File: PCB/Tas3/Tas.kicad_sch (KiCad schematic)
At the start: 28 parts, among them J1 Shelly 1, J2 Conn_01x07, J3 USB-C, U1 MD8942, U2 Barcode, U3 CH340X, U4 ZXGD3009E6, U5 ZXGD3009E6

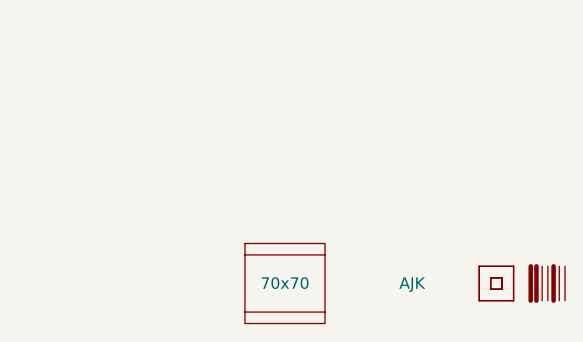
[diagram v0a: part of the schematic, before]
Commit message: Changed for cheaper assembly
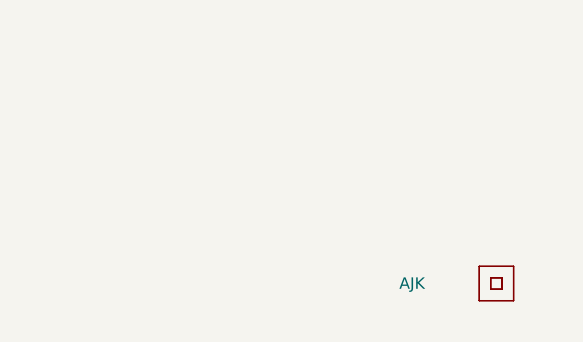
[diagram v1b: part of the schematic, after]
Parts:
- removed PCB1: 70x70, RevK:PCB7070, symbol RevK:PCB
- removed U2: Barcode, RevK:EAN-5060634238014, symbol RevK:Barcode
- removed V1, V2: ~, RevK:VCUT70, symbol RevK:VCUT
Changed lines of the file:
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@@
-    )
-  )
-  (symbol (lib_id "RevK:PCB") (at 245.745 172.72 0) (unit 1)
-    (in_bom no) (on_board yes) (dnp no)
-    (property "Reference" "PCB1" (at 245.745 182.88 0)
-      (effects (font (size 1.27 1.27)) hide)
-    )
-    (property "Value" "70x70" (at 245.745 172.72 0)
-      (effects (font (size 1.27 1.27)))
-    )
-    (property "Footprint" "RevK:PCB7070" (at 245.745 167.005 0)
-      (effects (font (size 1.27 1.27)) hide)
-    )
-    (property "Datasheet" "" (at 245.745 172.72 0)
-      (effects (font (size 1.27 1.27)) hide)
-    )
-    (instances
-      (project "Tas"
-        (path "/42713045-fffd-4b2d-ae1e-7232d705fb12"
-          (reference "PCB1") (unit 1)
-        )
-      )
     )
   )
@@
         (path "/825c70b0-4860-42b7-97dc-86bfa46e06fd"
           (reference "R8") (unit 1)
-        )
-      )
-    )
-  )
-  (symbol (lib_id "RevK:VCUT") (at 245.745 175.895 0) (unit 1)
-    (in_bom no) (on_board yes) (dnp no) (fields_autoplaced)
-    (property "Reference" "V1" (at 245.745 174.625 0)
-      (effects (font (size 1.27 1.27)) hide)
-    )
-    (property "Value" "~" (at 245.745 175.895 0)
-      (effects (font (size 1.27 1.27)))
-    )
-    (property "Footprint" "RevK:VCUT70" (at 245.745 177.165 0)
-      (effects (font (size 1.27 1.27)) hide)
-    )
-    (property "Datasheet" "" (at 245.745 175.895 0)
-      (effects (font (size 1.27 1.27)) hide)
-    )
-    (property "Sim.Enable" "0" (at 245.745 175.895 0)
-      (effects (font (size 1.27 1.27)) hide)
-    )
-    (instances
-      (project "Tas"
-        (path "/42713045-fffd-4b2d-ae1e-7232d705fb12"
-          (reference "V1") (unit 1)
-        )
-      )
-      (project "Reference"
-        (path "/825c70b0-4860-42b7-97dc-86bfa46e06fd"
-          (reference "V1") (unit 1)
-        )
-      )
-    )
-  )
-  (symbol (lib_id "RevK:VCUT") (at 245.745 169.545 0) (unit 1)
-    (in_bom no) (on_board yes) (dnp no) (fields_autoplaced)
-    (property "Reference" "V2" (at 245.745 168.275 0)
-      (effects (font (size 1.27 1.27)) hide)
-    )
-    (property "Value" "~" (at 245.745 169.545 0)
-      (effects (font (size 1.27 1.27)))
-    )
-    (property "Footprint" "RevK:VCUT70" (at 245.745 170.815 0)
-      (effects (font (size 1.27 1.27)) hide)
-    )
-    (property "Datasheet" "" (at 245.745 169.545 0)
-      (effects (font (size 1.27 1.27)) hide)
-    )
-    (property "Sim.Enable" "0" (at 245.745 169.545 0)
-      (effects (font (size 1.27 1.27)) hide)
-    )
-    (instances
-      (project "Tas"
-        (path "/42713045-fffd-4b2d-ae1e-7232d705fb12"
-          (reference "V2") (unit 1)
-        )
-      )
-      (project "Reference"
-        (path "/825c70b0-4860-42b7-97dc-86bfa46e06fd"
-          (reference "V1") (unit 1)
         )
       )
@@
         )
       )
-    )
-  )
-  (symbol (lib_id "RevK:Barcode") (at 274.955 172.72 0) (unit 1)
-    (in_bom no) (on_board yes) (dnp no) (fields_autoplaced)
-    (property "Reference" "U2" (at 274.955 175.895 0)
-      (effects (font (size 1.27 1.27)) hide)
-    )
-    (property "Value" "Barcode" (at 274.955 177.8 0)
-      (effects (font (size 1.27 1.27)) hide)
-    )
-    (property "Footprint" "RevK:EAN-5060634238014" (at 274.32 173.355 0)
-      (effects (font (size 1.27 1.27)) hide)
-    )
-    (property "Datasheet" "" (at 274.32 173.355 0)
-      (effects (font (size 1.27 1.27)) hide)
-    )
-    (property "Note" "Non part, PCB printed" (at 274.955 167.005 0)
-      (effects (font (size 1.27 1.27)) hide)
-    )
-    (instances
-      (project "USBA"
-        (path "/2d210a96-f81f-42a9-8bf4-1b43c11086f3"
-          (reference "U2") (unit 1)
-        )
-      )
-      (project "Tas"
-        (path "/42713045-fffd-4b2d-ae1e-7232d705fb12"
-          (reference "U2") (unit 1)
-        )
-      )
-      (project "Faikin"
-        (path "/46c350bb-7de4-4e81-aafd-4af55e37aab0"
-          (reference "U4") (unit 1)
-        )
-      )
-      (project "Reference"
-        (path "/825c70b0-4860-42b7-97dc-86bfa46e06fd"
-          (reference "U3") (unit 1)
-        )
-      )

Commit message: Changed voltage...
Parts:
- R4: value 40k2 -> 34k4
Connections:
- net RST+: now also J2.4 (Pin_4)
- net VBUS: now also U3.7 (VCC)
- net +3V3 renamed +3V8
- net +3V8: no longer C5.1, J2.4 (Pin_4), U3.10 (V3), U3.7 (VCC)
- new net: C5.1, U3.10 (V3)
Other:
- note added: "Aiming for 3.8V due to driver drop"
- note added: "DOES NOT WORK AT 3V3 The 0.8 to 0.4 drop on high and 0.2 to 0.5 on low are an issue. Low is probably OK, but high means needs drive of at least 0.5V higher. Measured was 0.45V drop."
- note added: "New resistor values"
- moved on the sheet: C5

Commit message: Try again, as ordered.
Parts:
- removed U4, U5: ZXGD3009E6, RevK:SOT-23-6, symbol Driver_FET:ZXGD3009E6
- added Q1: AP2003, RevK:SOT-23-6, symbol Transistor_FET:DMC3071LVT
- added U2: 74LVC1G07, RevK:SOT-353_SC-70-5, symbol 74xGxx:NC7SZ125M5X
- added U4: 74LVC1G06SE-7, RevK:SOT-353_SC-70-5, symbol 74xGxx:NC7SVU04P5X
- D1: JLCPCB Rotation Offset -90 -> 0; LCSC Part # C68987 -> C96225
- R4: value 34k4 -> 39k2
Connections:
- net +3V8 is gone; now on net +3V3: D1.2 (K2), D1.5 (K4), D5.4 (A), U1.8 (VOUT)
- net B: now also U2.4 (Y)
- net GND: now also Q1.5 (S), U2.1 (~{OE}), U2.3 (GND), U4.3 (GND)
- net GPIO0: now also U2.2 (A)
- net RST: now also U4.2
- net RST+: now also Q1.4 (D), Q1.6 (D); no longer J2.4 (Pin_4)
- net VBUS: no longer U3.7 (VCC)
- net +3V3: now reaches C5.1, U3.10 (V3)
- net +3V3: now also J2.4 (Pin_4), U3.7 (VCC), Q1.2 (S), U2.5 (VCC), U4.5 (VCC)
- new net: Q1.1 (G), Q1.3 (G), U4.4
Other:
- note removed: "Aiming for 3.8V due to driver drop"
- note removed: "Cannot connect GPIO0 directly as internal pulls in shelly upset CH340X"
- note removed: "DOES NOT WORK AT 3V3 The 0.8 to 0.4 drop on high and 0.2 to 0.5 on low are an issue. Low is probably OK, but high means needs drive of at least 0.5V higher. Measured was 0.45V drop."
- note removed: "New resistor values"
- moved on the sheet: C1, C5, C6, C7, D1A, D1B, D5, J1, J2, J3, L2, R1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

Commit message: Maybe Nth time lucky
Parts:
- added C2: 100nF, RevK:C_0402, symbol Device:C
- added R5, R6: 4K7, RevK:R_0402, symbol Device:R
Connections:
- net +3V3: now also R5.1, R6.1; no longer U3.10 (V3), U3.7 (VCC)
- net B: now also R6.2
- net GND: now also C2.1
- net VBUS: now also U3.7 (VCC)
- net at Q1.1 (G), Q1.3 (G), U4.4: now also R5.2
- new net: C2.2, U3.10 (V3)
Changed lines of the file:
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@@
   (junction (at 239.395 123.19) (diameter 0) (color 0 0 0 0)
   )
+  (junction (at 191.77 123.19) (diameter 0) (color 0 0 0 0)
+  )
   (junction (at 134.62 70.485) (diameter 0) (color 0 0 0 0)
   )
   (junction (at 150.495 131.445) (diameter 0) (color 0 0 0 0)
   )
-  (junction (at 140.335 109.855) (diameter 0) (color 0 0 0 0)
+  (junction (at 239.395 113.03) (diameter 0) (color 0 0 0 0)
   )
   (junction (at 163.83 38.735) (diameter 0) (color 0 0 0 0)
@@
     (stroke (width 0) (type default))
   )
+  (wire (pts (xy 139.065 103.505) (xy 139.065 109.855))
+    (stroke (width 0) (type default))
+  )
   (wire (pts (xy 163.83 37.465) (xy 163.83 38.735))
     (stroke (width 0) (type default))
@@
     (stroke (width 0) (type default))
   )
-  (wire (pts (xy 139.065 109.855) (xy 140.335 109.855))
-    (stroke (width 0) (type default))
-  )
   (wire (pts (xy 153.67 40.005) (xy 156.21 40.005))
     (stroke (width 0) (type default))
   )
+  (wire (pts (xy 191.77 123.19) (xy 191.77 120.015))
+    (stroke (width 0) (type default))
+  )
+  (wire (pts (xy 239.395 107.95) (xy 239.395 113.03))
+    (stroke (width 0) (type default))
+  )
   (wire (pts (xy 239.395 113.03) (xy 239.395 123.19))
     (stroke (width 0) (type default))
@@
     (stroke (width 0) (type default))
   )
-  (wire (pts (xy 140.335 109.855) (xy 141.605 109.855))
+  (wire (pts (xy 150.495 131.445) (xy 151.765 131.445))
     (stroke (width 0) (type default))
   )
-  (wire (pts (xy 150.495 131.445) (xy 151.765 131.445))
+  (wire (pts (xy 191.77 123.19) (xy 193.04 123.19))
     (stroke (width 0) (type default))
   )
@@
     )
   )
-  (global_label "GPIO0+" (shape output) (at 191.77 123.19 0) (fields_autoplaced)
+  (global_label "GPIO0+" (shape output) (at 193.04 123.19 0) (fields_autoplaced)
     (effects (font (size 1.27 1.27)) (justify left))
-    (property "Intersheetrefs" "${INTERSHEET_REFS}" (at 201.2788 123.19 0)
+    (property "Intersheetrefs" "${INTERSHEET_REFS}" (at 202.5488 123.19 0)
       (effects (font (size 1.27 1.27)) (justify left) hide)
     )
@@
     (property "Intersheetrefs" "${INTERSHEET_REFS}" (at 82.5663 60.325 0)
       (effects (font (size 1.27 1.27)) (justify right) hide)
+    )
+  )
+  (global_label "VBUS" (shape input) (at 141.605 109.855 90) (fields_autoplaced)
+    (effects (font (size 1.27 1.27)) (justify left))
+    (property "Intersheetrefs" "${INTERSHEET_REFS}" (at 141.605 102.7048 90)
+      (effects (font (size 1.27 1.27)) (justify left) hide)
     )
   )
@@
   (symbol (lib_id "74xGxx:NC7SZ125M5X") (at 181.61 125.73 0) (unit 1)
     (in_bom yes) (on_board yes) (dnp no)
-    (property "Reference" "U2" (at 187.96 116.84 0)
-      (effects (font (size 1.27 1.27)))
-    )
-    (property "Value" "74LVC1G07" (at 187.96 118.888 0)
+    (property "Reference" "U2" (at 187.96 133.207 0)
+      (effects (font (size 1.27 1.27)))
+    )
+    (property "Value" "74LVC1G07" (at 187.96 135.255 0)
       (effects (font (size 1.27 1.27)))
     )
@@
         (path "/42713045-fffd-4b2d-ae1e-7232d705fb12"
           (reference "#PWR026") (unit 1)
+        )
+      )
+    )
+  )
+  (symbol (lib_id "Device:C") (at 139.065 99.695 0) (unit 1)
+    (in_bom yes) (on_board yes) (dnp no) (fields_autoplaced)
+    (property "Reference" "C2" (at 141.986 98.8603 0)
+      (effects (font (size 1.27 1.27)) (justify left))
+    )
+    (property "Value" "100nF" (at 141.986 101.3972 0)
+      (effects (font (size 1.27 1.27)) (justify left))
+    )
+    (property "Footprint" "RevK:C_0402" (at 140.0302 103.505 0)
+      (effects (font (size 1.27 1.27)) hide)
+    )
+    (property "Datasheet" "~" (at 139.065 99.695 0)
+      (effects (font (size 1.27 1.27)) hide)
+    )
+    (pin "1")
+    (pin "2")
+    (instances
+      (project "Tas"
+        (path "/42713045-fffd-4b2d-ae1e-7232d705fb12"
+          (reference "C2") (unit 1)
         )
       )
@@
     )
   )
+  (symbol (lib_id "power:+3V3") (at 191.77 112.395 0) (unit 1)
+    (in_bom yes) (on_board yes) (dnp no) (fields_autoplaced)
+    (property "Reference" "#PWR022" (at 191.77 116.205 0)
+      (effects (font (size 1.27 1.27)) hide)
+    )
+    (property "Value" "+3V3" (at 191.77 108.45 0)
+      (effects (font (size 1.27 1.27)))
+    )
+    (property "Footprint" "" (at 191.77 112.395 0)
+      (effects (font (size 1.27 1.27)) hide)
+    )
+    (property "Datasheet" "" (at 191.77 112.395 0)
+      (effects (font (size 1.27 1.27)) hide)
+    )
+    (pin "1")
+    (instances
+      (project "Tas"
+        (path "/42713045-fffd-4b2d-ae1e-7232d705fb12"
+          (reference "#PWR022") (unit 1)
+        )
+      )
+    )
+  )
   (symbol (lib_id "RevK:Hidden") (at 232.41 34.29 0) (unit 1)
     (in_bom yes) (on_board yes) (dnp no)
@@
     )
   )
+  (symbol (lib_id "power:+3V3") (at 239.395 100.33 0) (unit 1)
+    (in_bom yes) (on_board yes) (dnp no) (fields_autoplaced)
+    (property "Reference" "#PWR021" (at 239.395 104.14 0)
+      (effects (font (size 1.27 1.27)) hide)
+    )
+    (property "Value" "+3V3" (at 239.395 96.385 0)
+      (effects (font (size 1.27 1.27)))
+    )
+    (property "Footprint" "" (at 239.395 100.33 0)
+      (effects (font (size 1.27 1.27)) hide)
+    )
+    (property "Datasheet" "" (at 239.395 100.33 0)
+      (effects (font (size 1.27 1.27)) hide)
+    )
+    (pin "1")
+    (instances
+      (project "Tas"
+        (path "/42713045-fffd-4b2d-ae1e-7232d705fb12"
+          (reference "#PWR021") (unit 1)
+        )
+      )
+    )
+  )
   (symbol (lib_id "RevK:Hidden") (at 232.41 38.1 90) (unit 1)
     (in_bom yes) (on_board yes) (dnp no)
@@
     )
   )
-  (symbol (lib_id "power:+3V3") (at 140.335 109.855 0) (unit 1)
+  (symbol (lib_id "power:GND") (at 139.065 95.885 180) (unit 1)
     (in_bom yes) (on_board yes) (dnp no) (fields_autoplaced)
-    (property "Reference" "#PWR08" (at 140.335 113.665 0)
-      (effects (font (size 1.27 1.27)) hide)
-    )
-    (property "Value" "+3V3" (at 140.335 105.91 0)
-      (effects (font (size 1.27 1.27)))
-    )
-    (property "Footprint" "" (at 140.335 109.855 0)
-      (effects (font (size 1.27 1.27)) hide)
-    )
-    (property "Datasheet" "" (at 140.335 109.855 0)
+    (property "Reference" "#PWR08" (at 139.065 89.535 0)
+      (effects (font (size 1.27 1.27)) hide)
+    )
+    (property "Value" "GND" (at 139.065 91.94 0)
+      (effects (font (size 1.27 1.27)))
+    )
+    (property "Footprint" "" (at 139.065 95.885 0)
+      (effects (font (size 1.27 1.27)) hide)
+    )
+    (property "Datasheet" "" (at 139.065 95.885 0)
       (effects (font (size 1.27 1.27)) hide)
     )
@@
     )
   )
+  (symbol (lib_id "Device:R") (at 239.395 104.14 0) (unit 1)
+    (in_bom yes) (on_board yes) (dnp no)
+    (property "Reference" "R5" (at 241.3 104.14 90)
+      (effects (font (size 1.27 1.27)))
+    )
+    (property "Value" "4K7" (at 239.395 104.14 90)
+      (effects (font (size 1.27 1.27)))
+    )
+    (property "Footprint" "RevK:R_0402" (at 237.617 104.14 90)
+      (effects (font (size 1.27 1.27)) hide)
+    )
+    (property "Datasheet" "~" (at 239.395 104.14 0)
+      (effects (font (size 1.27 1.27)) hide)
+    )
+    (pin "1")
+    (pin "2")
+    (instances
+      (project "Tas"
+        (path "/42713045-fffd-4b2d-ae1e-7232d705fb12"
+          (reference "R5") (unit 1)
+        )
+      )
+      (project "Generic6"
+        (path "/46c350bb-7de4-4e81-aafd-4af55e37aab0"
+          (reference "R2") (unit 1)
+        )
+      )
+      (project "Reference"
+        (path "/825c70b0-4860-42b7-97dc-86bfa46e06fd"
+          (reference "R7") (unit 1)
+        )
+      )
+    )
+  )
   (symbol (lib_id "power:+3V3") (at 113.665 121.285 0) (unit 1)
     (in_bom yes) (on_board yes) (dnp no) (fields_autoplaced)
@@
         )
       )
+    )
+  )
+  (symbol (lib_id "Device:R") (at 191.77 116.205 0) (unit 1)
+    (in_bom yes) (on_board yes) (dnp no)
+    (property "Reference" "R6" (at 193.675 116.205 90)
+      (effects (font (size 1.27 1.27)))
+    )
+    (property "Value" "4K7" (at 191.77 116.205 90)
+      (effects (font (size 1.27 1.27)))
+    )
+    (property "Footprint" "RevK:R_0402" (at 189.992 116.205 90)
+      (effects (font (size 1.27 1.27)) hide)
+    )
+    (property "Datasheet" "~" (at 191.77 116.205 0)
+      (effects (font (size 1.27 1.27)) hide)
+    )
+    (pin "1")
+    (pin "2")
+    (instances
+      (project "Tas"
+        (path "/42713045-fffd-4b2d-ae1e-7232d705fb12"
+          (reference "R6") (unit 1)
+        )
+      )
+      (project "Generic6"
+        (path "/46c350bb-7de4-4e81-aafd-4af55e37aab0"
+          (reference "R2") (unit 1)
+        )
+      )
+      (project "Reference"
+        (path "/825c70b0-4860-42b7-97dc-86bfa46e06fd"
+          (reference "R7") (unit 1)
+        )
+      )
